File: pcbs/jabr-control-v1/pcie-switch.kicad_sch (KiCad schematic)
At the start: 1 part, among them U3001 PI7C9X2G303EL

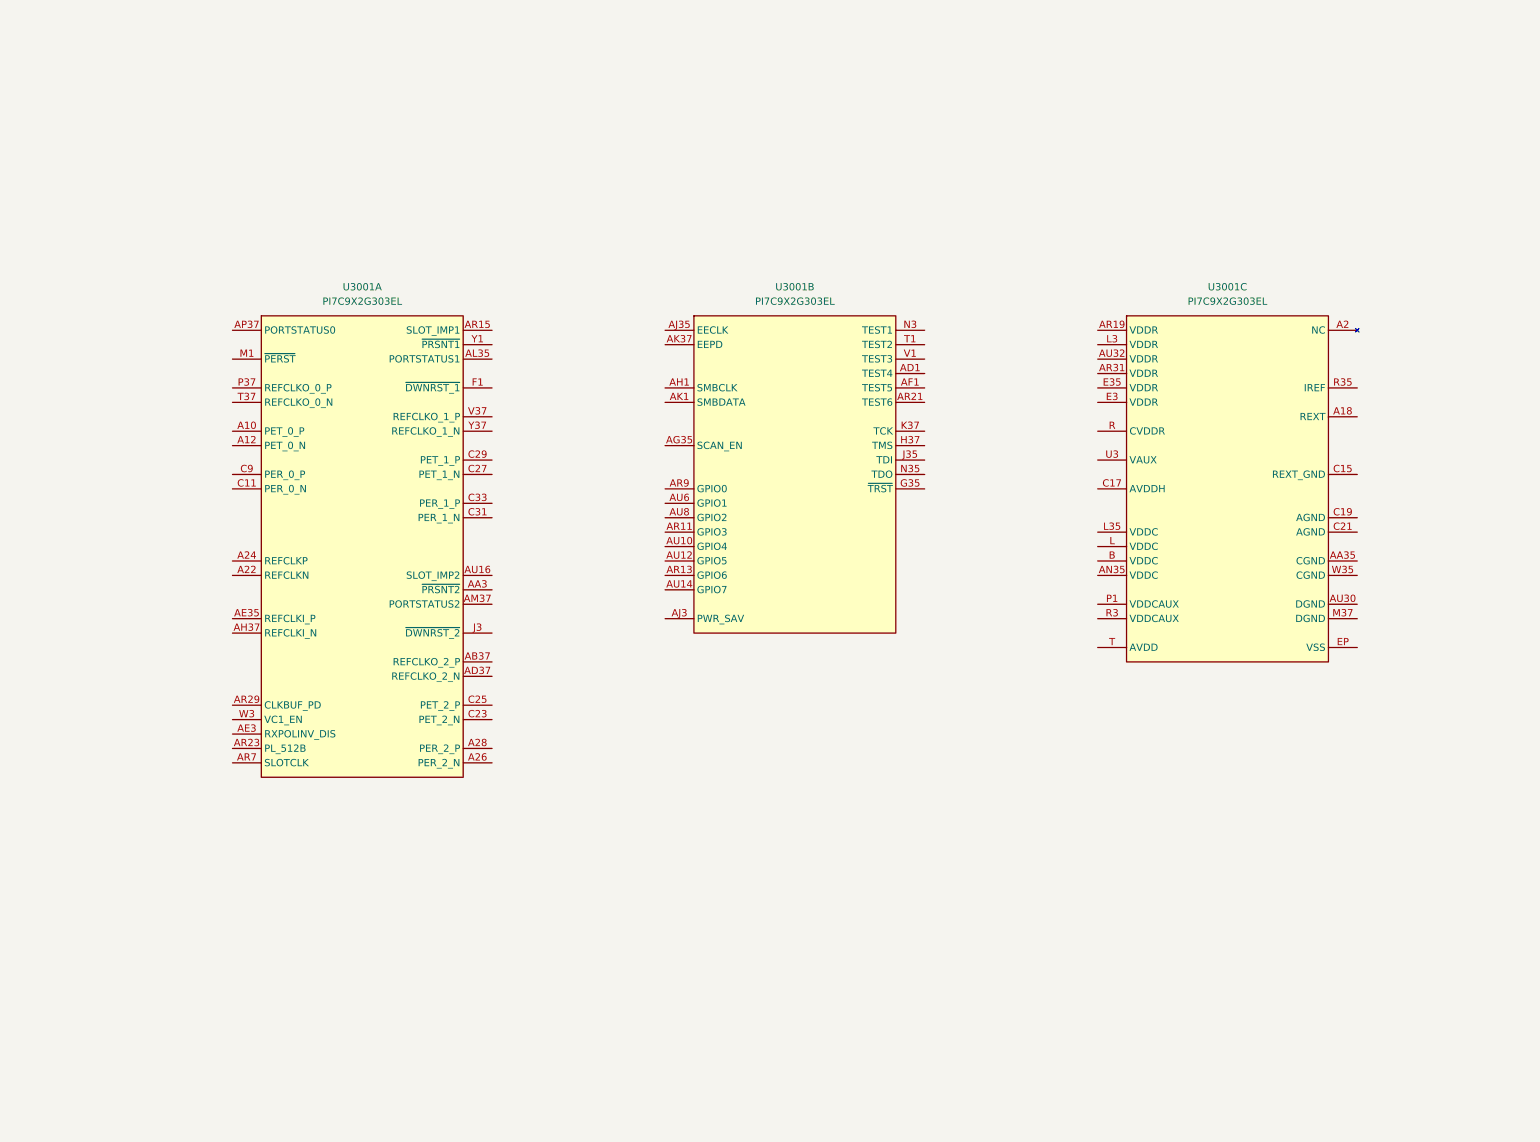
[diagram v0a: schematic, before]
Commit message: Added PCIe connections
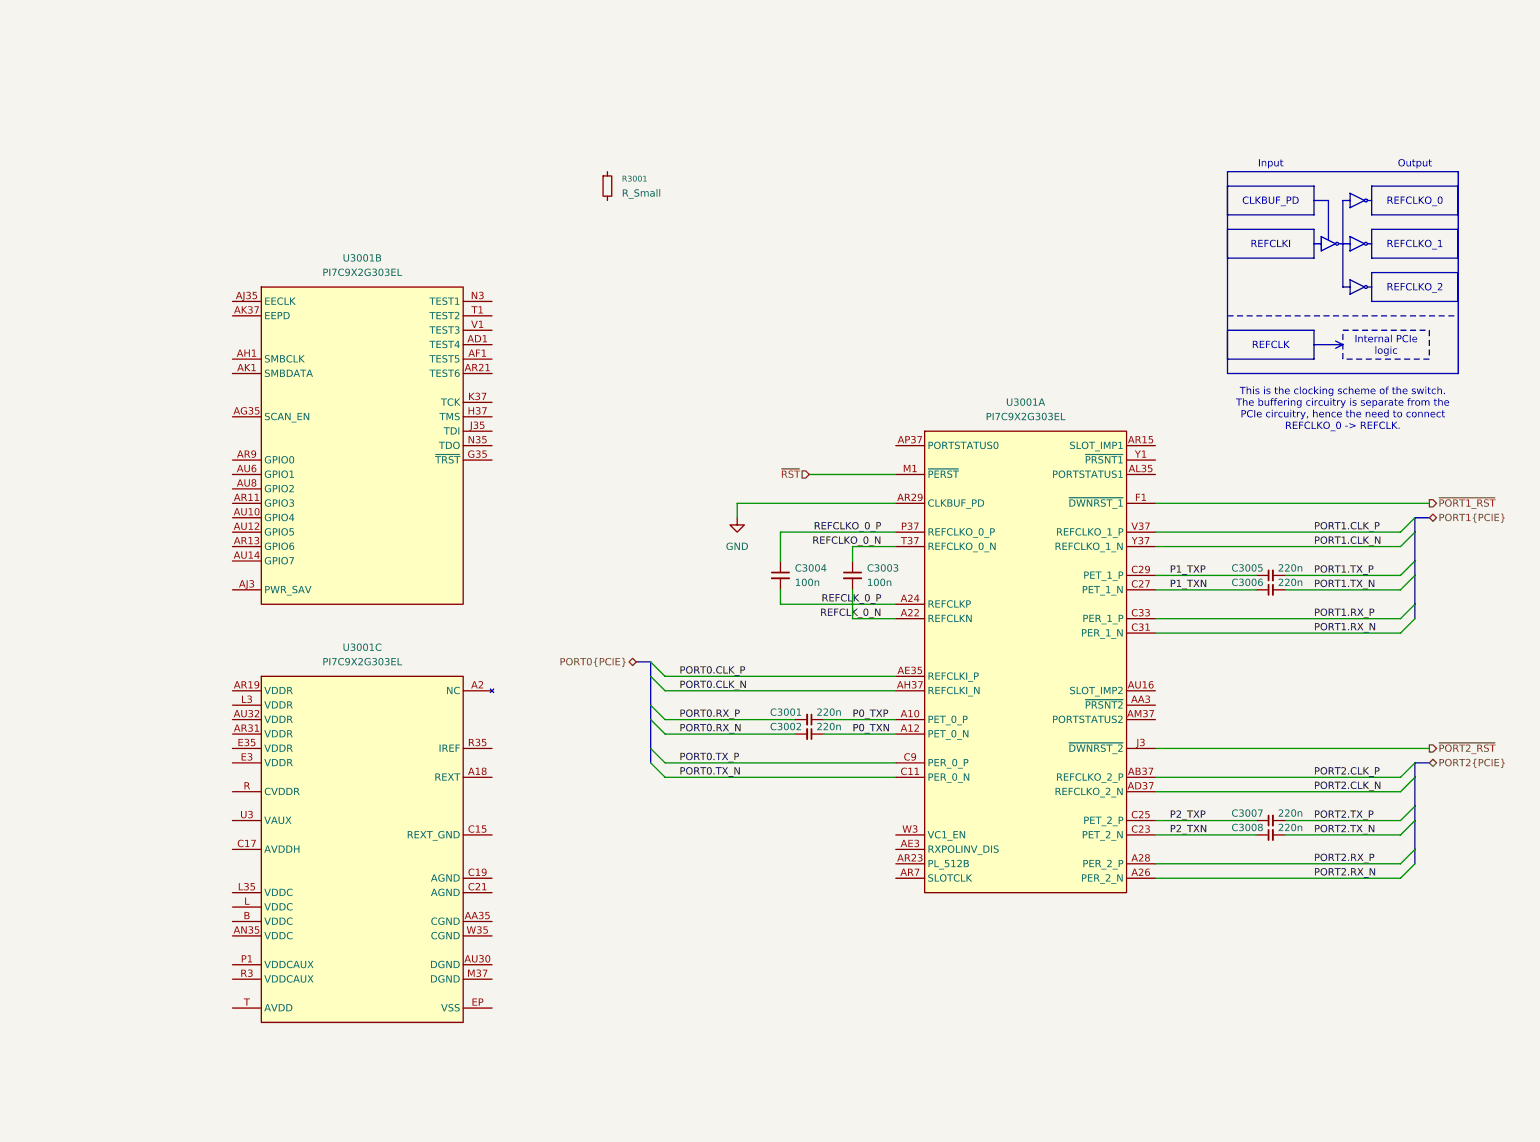
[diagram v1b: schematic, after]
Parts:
- added C3001, C3002, C3005, C3006, C3007, C3008: 220n, project_footprints:C_0402, symbol DEV:C_TINY_IO
- added C3003, C3004: 100n, project_footprints:C_0402, symbol DEV:C_SMALL_IO
- added R3001: R_Small, project_footprints:R_0402, symbol Device:R_Small
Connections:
- net P0_TXP: now reaches U3001.A10 (PET_0_P)
- net P0_TXP: now also C3001.1
- net P0_TXN: now reaches U3001.A12 (PET_0_N)
- net P0_TXN: now also C3002.1
- net REFCLK_0_N: now reaches U3001.A22 (REFCLKN)
- net REFCLK_0_N: now also C3003.2
- net REFCLK_0_P: now reaches U3001.A24 (REFCLKP)
- net REFCLK_0_P: now also C3004.2
- net PORT2.RX_N: now reaches U3001.A26 (PER_2_N)
- net PORT2.RX_P: now reaches U3001.A28 (PER_2_P)
- net PORT2.CLK_P: now reaches U3001.AB37 (REFCLKO_2_P)
- net PORT2.CLK_N: now reaches U3001.AD37 (REFCLKO_2_N)
- net PORT0.CLK_P: now reaches U3001.AE35 (REFCLKI_P)
- net PORT0.CLK_N: now reaches U3001.AH37 (REFCLKI_N)
- net GND: now reaches U3001.AR29 (CLKBUF_PD)
- net PORT0.TX_N: now reaches U3001.C11 (PER_0_N)
- net P2_TXN: now reaches U3001.C23 (PET_2_N)
- net P2_TXN: now also C3008.1
- net P2_TXP: now reaches U3001.C25 (PET_2_P)
- net P2_TXP: now also C3007.1
- net P1_TXN: now reaches U3001.C27 (PET_1_N)
- net P1_TXN: now also C3006.1
- net P1_TXP: now reaches U3001.C29 (PET_1_P)
- net P1_TXP: now also C3005.1
- net PORT1.RX_N: now reaches U3001.C31 (PER_1_N)
- net PORT1.RX_P: now reaches U3001.C33 (PER_1_P)
- net PORT0.TX_P: now reaches U3001.C9 (PER_0_P)
- net ~{PORT1_RST}: now reaches U3001.F1 (~{DWNRST_1})
- net ~{PORT2_RST}: now reaches U3001.J3 (~{DWNRST_2})
- net ~{RST}: now reaches U3001.M1 (~{PERST})
- net REFCLKO_0_P: now reaches U3001.P37 (REFCLKO_0_P)
- net REFCLKO_0_P: now also C3004.1
- net REFCLKO_0_N: now reaches U3001.T37 (REFCLKO_0_N)
- net REFCLKO_0_N: now also C3003.1
- net PORT1.CLK_P: now reaches U3001.V37 (REFCLKO_1_P)
- net PORT1.CLK_N: now reaches U3001.Y37 (REFCLKO_1_N)
- new net PORT0.RX_N: C3002.2
- new net PORT0.RX_P: C3001.2
- new net PORT1.TX_N: C3006.2
- new net PORT1.TX_P: C3005.2
- new net PORT2.TX_N: C3008.2
- new net PORT2.TX_P: C3007.2
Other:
- note added: "Input"
- note added: "Output"
- note added: "This is the clocking scheme of the switch. The buffering circuitry is separate from the PCIe circuitry, hence the need to connect REFCLKO_0 -> REFCLK."
- moved on the sheet: U3001A, U3001B, U3001C

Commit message: Added power sheets
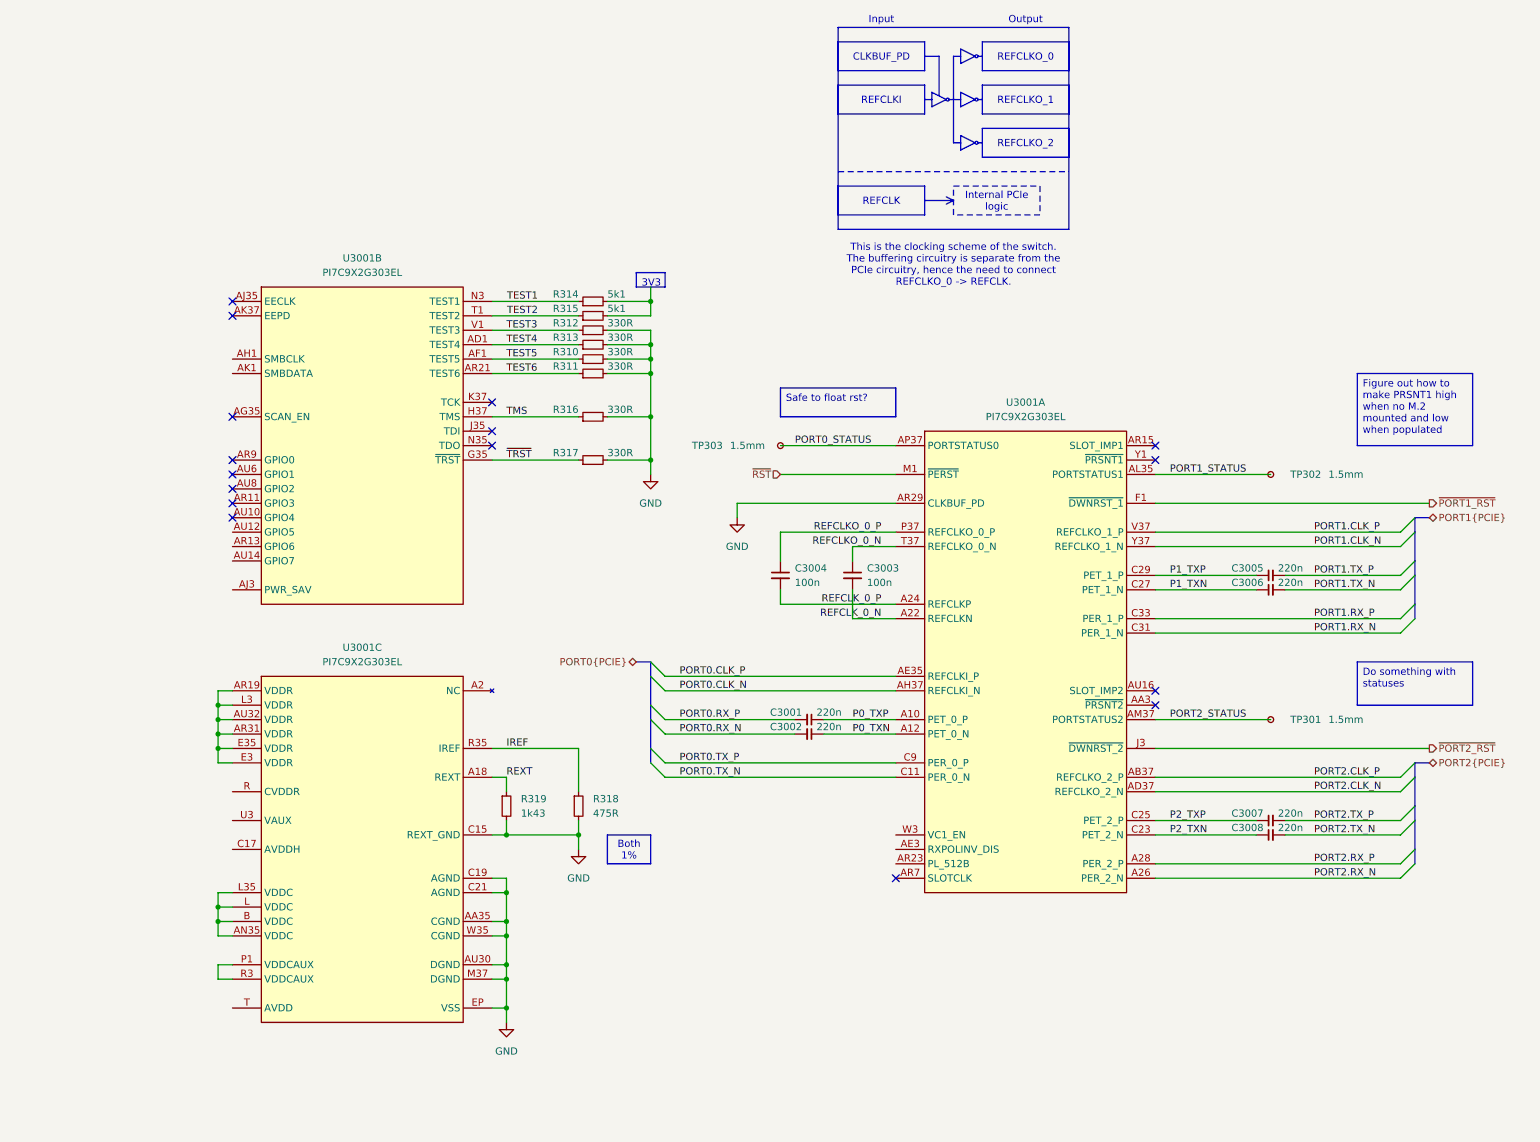
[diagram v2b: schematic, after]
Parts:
- removed R3001: R_Small, project_footprints:R_0402, symbol Device:R_Small
- added R310, R311, R312, R313, R316, R317: 330R, symbol DEV:R_SMALL
- added R314, R315: 5k1, symbol DEV:R_SMALL
- added R318: 475R, project_footprints:R_0402, symbol DEV:R_SMALL
- added R319: 1k43, project_footprints:R_0402, symbol DEV:R_SMALL
- added TP301, TP302, TP303: 1.5mm, TestPoint:TestPoint_Pad_D1.5mm, symbol Connector:TestPoint_Small
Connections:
- net GND: now also U3001.AA35 (CGND), U3001.AU30 (DGND), U3001.C15 (REXT_GND), U3001.C19 (AGND), U3001.C21 (AGND), U3001.EP (VSS), U3001.M37 (DGND), U3001.W35 (CGND), R310.2, R311.2, R312.2, R313.2, R316.2, R317.2, R318.2, R319.2
- net PORT1_STATUS: now reaches U3001.AL35 (PORTSTATUS1)
- net PORT1_STATUS: now also TP302.1
- net PORT2_STATUS: now reaches U3001.AM37 (PORTSTATUS2)
- net PORT2_STATUS: now also TP301.1
- net PORT0_STATUS: now reaches U3001.AP37 (PORTSTATUS0)
- net PORT0_STATUS: now also TP303.1
- net REXT: now reaches U3001.A18 (REXT)
- net REXT: now also R319.1
- net at U3001.AN35 (VDDC): now also U3001.B (VDDC), U3001.L (VDDC), U3001.L35 (VDDC)
- net at U3001.AR19 (VDDR): now also U3001.AR31 (VDDR), U3001.AU32 (VDDR), U3001.E3 (VDDR), U3001.E35 (VDDR), U3001.L3 (VDDR)
- net at U3001.P1 (VDDCAUX): now also U3001.R3 (VDDCAUX)
- net IREF: now reaches U3001.R35 (IREF)
- net IREF: now also R318.1
- net TEST4: now reaches U3001.AD1 (TEST4)
- net TEST4: now also R313.1
- net TEST5: now reaches U3001.AF1 (TEST5)
- net TEST5: now also R310.1
- net TEST6: now reaches U3001.AR21 (TEST6)
- net TEST6: now also R311.1
- net ~{TRST}: now reaches U3001.G35 (~{TRST})
- net ~{TRST}: now also R317.1
- net TMS: now reaches U3001.H37 (TMS)
- net TMS: now also R316.1
- net TEST1: now reaches U3001.N3 (TEST1)
- net TEST1: now also R314.1
- net TEST2: now reaches U3001.T1 (TEST2)
- net TEST2: now also R315.1
- net TEST3: now reaches U3001.V1 (TEST3)
- net TEST3: now also R312.1
- new net: R314.2, R315.2
- no-connect marks 0 -> 16

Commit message: Worked on power and other areas of the schematic
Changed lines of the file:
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@@
+		)
+	)
+	(text_box "CHANGE TO ASM1182e"
+		(exclude_from_sim no)
+		(at 83.82 12.7 0)
+		(size 45.72 22.86)
+		(margins 0.9525 0.9525 0.9525 0.9525)
+		(stroke
+			(width 0)
+			(type solid)
+			(color 255 0 0 1)
+		)
+		(fill
+			(type none)
+		)
+		(effects
+			(font
+				(size 5 5)
+				(color 255 0 0 1)
+			)
+			(justify left)
 		)
 	)

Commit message: Updated README
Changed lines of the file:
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@@
 		)
 	)
-	(text_box "CHANGE TO ASM1182e"
+	(text_box "CHANGE TO QFP-128 package"
 		(exclude_from_sim no)
-		(at 83.82 12.7 0)
-		(size 45.72 22.86)
+		(at 83.82 10.16 0)
+		(size 53.34 25.4)
 		(margins 0.9525 0.9525 0.9525 0.9525)
 		(stroke
